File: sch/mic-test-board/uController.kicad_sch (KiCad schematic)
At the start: 43 parts, among them J1 CN11.male, J12 CN12.female, J5 CN12.male, J6 CN11.female, U34 SN74LVC126ARGYR, U5 NUCLEO144-H743ZI

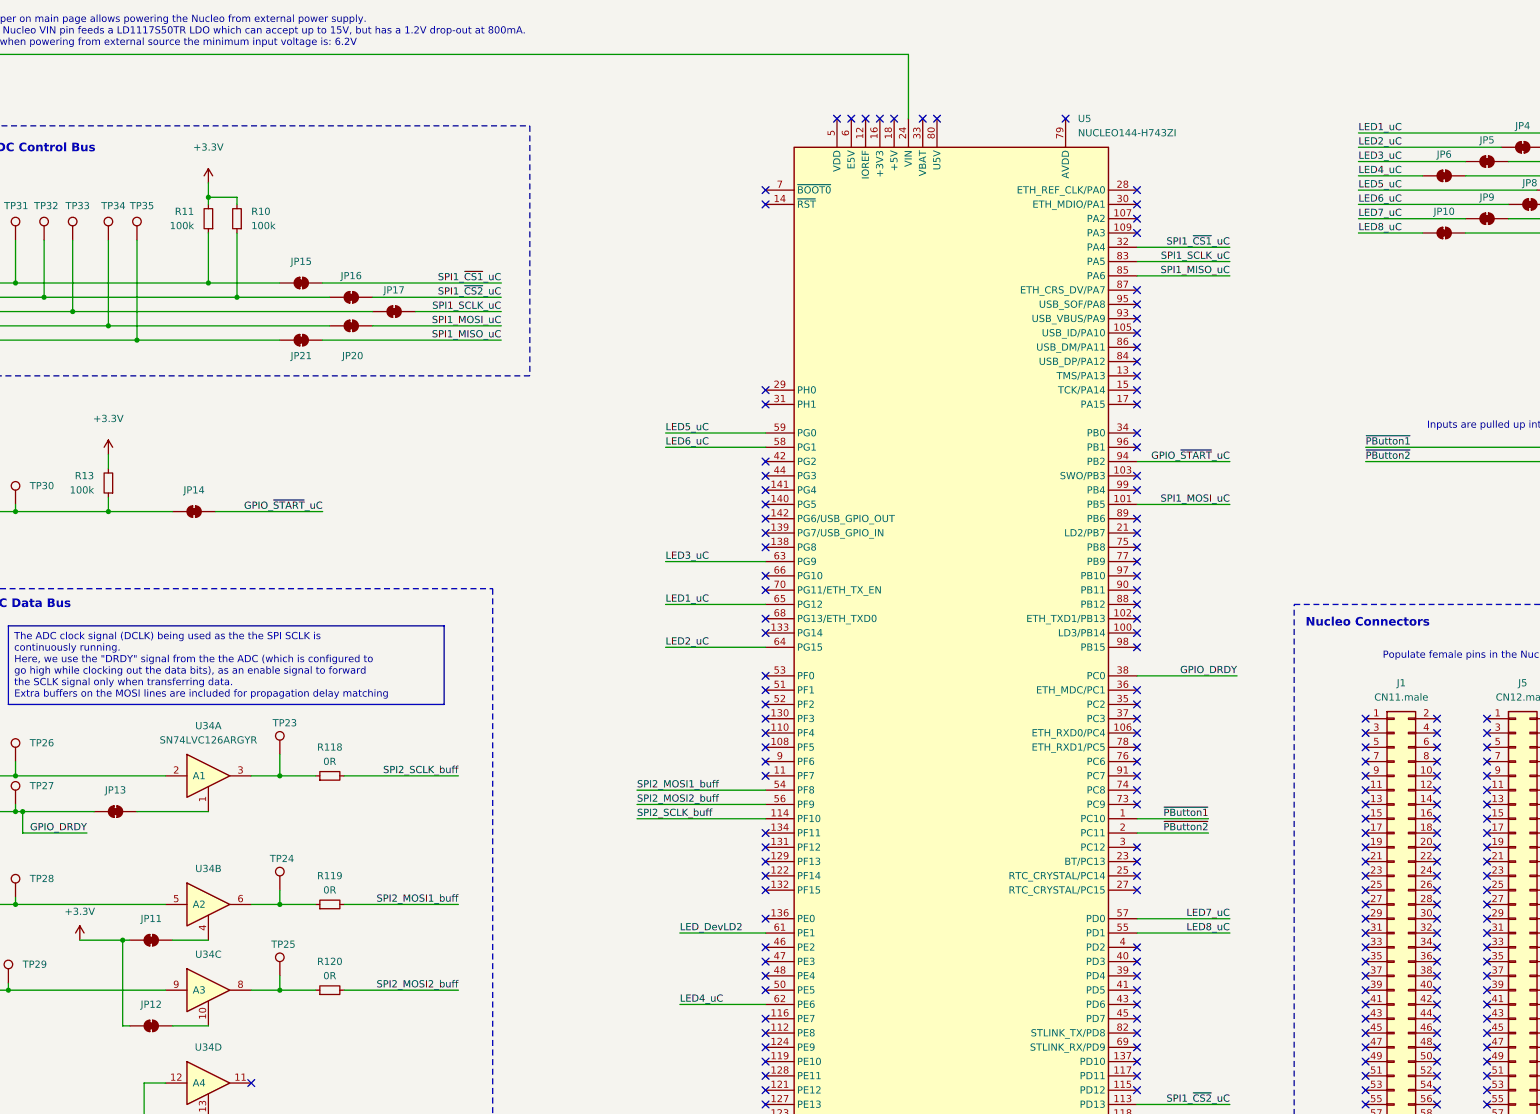
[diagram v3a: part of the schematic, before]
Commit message: sch: adding bringup notes
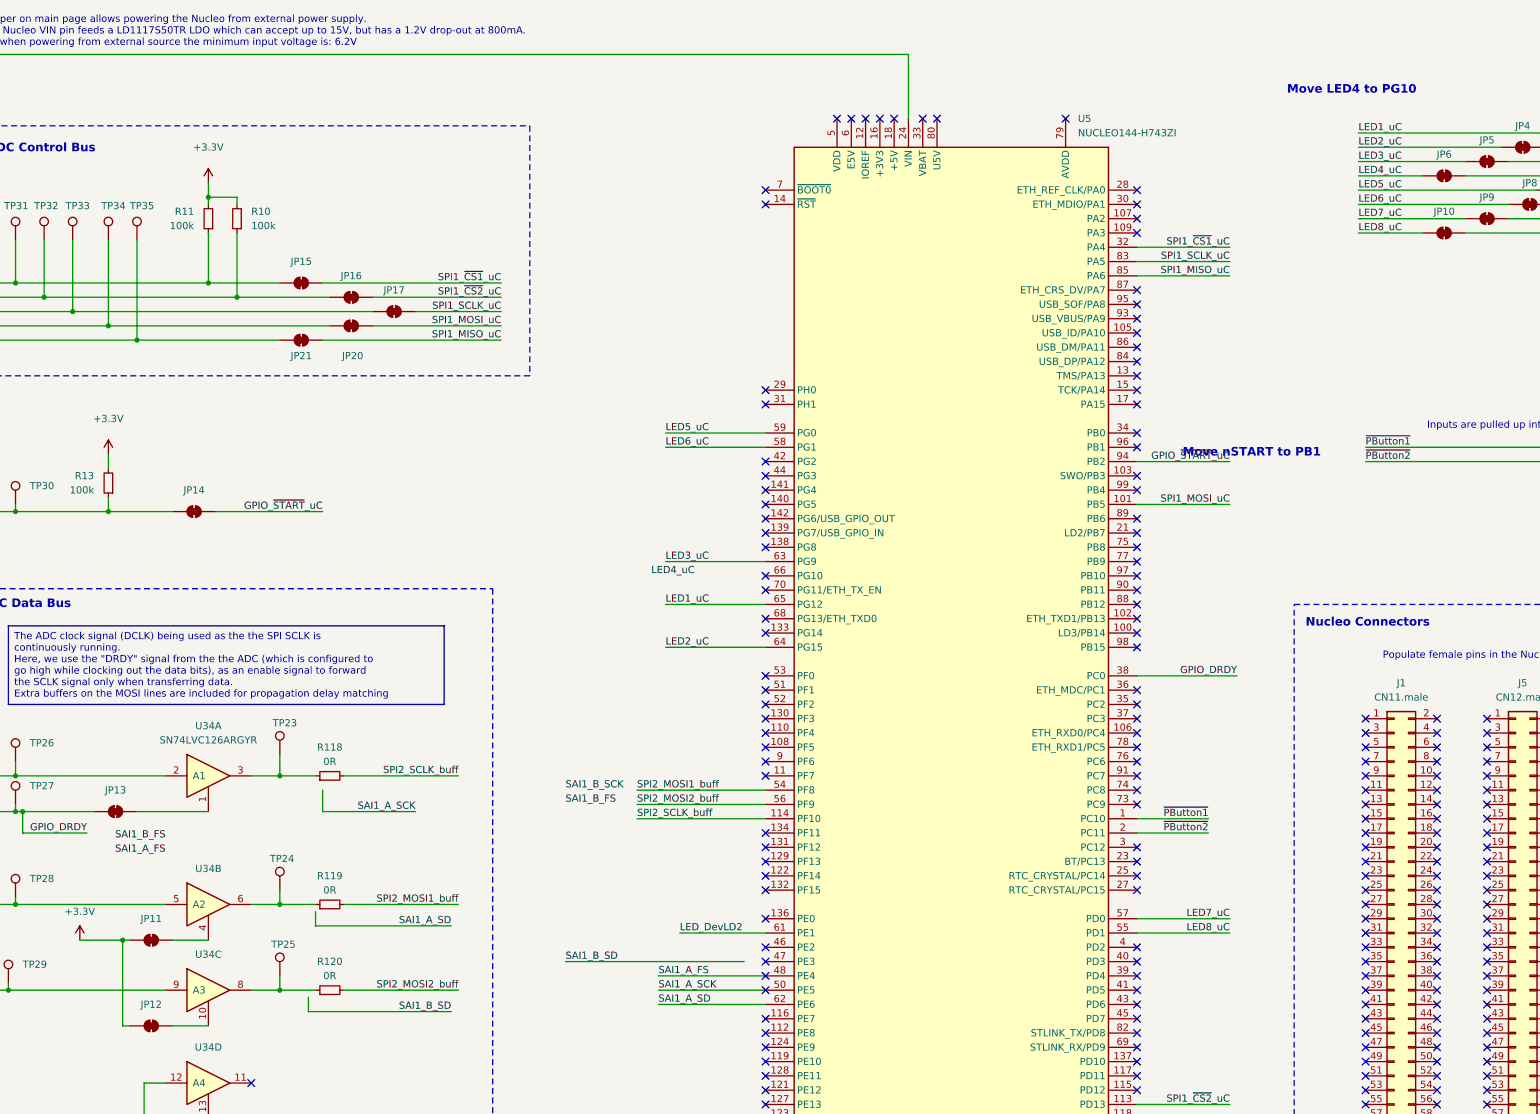
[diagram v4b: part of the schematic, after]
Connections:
- net LED4_uC: no longer U5.62 (PE6)
- net SAI1_A_FS: now reaches U5.48 (PE4)
- net SAI1_A_SCK: now reaches U5.50 (PE5)
- new net SAI1_A_SD: U5.62 (PE6)
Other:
- note added: "Move LED4 to PG10"
- note added: "Move nSTART to PB1"
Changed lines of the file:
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@@
+	(wire
+		(pts
+			(xy 170.18 190.5) (xy 201.93 190.5)
+		)
+		(stroke
+			(width 0)
+			(type default)
+		)
+	)
 	(wire
 		(pts
@@
 	(wire
 		(pts
+			(xy 127 160.02) (xy 127 163.83)
+		)
+		(stroke
+			(width 0)
+			(type default)
+		)
+	)
+	(wire
+		(pts
 			(xy 350.52 53.34) (xy 354.33 53.34)
 		)
@@
 	(wire
 		(pts
+			(xy 186.69 193.04) (xy 205.74 193.04)
+		)
+		(stroke
+			(width 0)
+			(type default)
+		)
+	)
+	(wire
+		(pts
 			(xy 182.88 162.56) (xy 205.74 162.56)
 		)
@@
 	(wire
 		(pts
+			(xy 186.69 195.58) (xy 205.74 195.58)
+		)
+		(stroke
+			(width 0)
+			(type default)
+		)
+	)
+	(wire
+		(pts
 			(xy 248.92 233.68) (xy 248.92 236.22)
 		)
@@
 	(wire
 		(pts
+			(xy 124.46 196.85) (xy 124.46 199.39)
+		)
+		(stroke
+			(width 0)
+			(type default)
+		)
+	)
+	(wire
+		(pts
 			(xy 72.39 162.56) (xy 72.39 163.83)
 		)
@@
 	(wire
 		(pts
+			(xy 149.86 184.15) (xy 125.73 184.15)
+		)
+		(stroke
+			(width 0)
+			(type default)
+		)
+	)
+	(wire
+		(pts
+			(xy 149.86 199.39) (xy 124.46 199.39)
+		)
+		(stroke
+			(width 0)
+			(type default)
+		)
+	)
+	(wire
+		(pts
 			(xy 95.25 212.09) (xy 95.25 218.44)
 		)
@@
 	(wire
 		(pts
-			(xy 190.5 198.12) (xy 205.74 198.12)
+			(xy 186.69 198.12) (xy 205.74 198.12)
 		)
 		(stroke
@@
 	(wire
 		(pts
+			(xy 125.73 181.61) (xy 125.73 184.15)
+		)
+		(stroke
+			(width 0)
+			(type default)
+		)
+	)
+	(wire
+		(pts
 			(xy 71.12 194.31) (xy 71.12 195.58)
 		)
@@
 		(pts
 			(xy 43.18 273.05) (xy 45.72 273.05)
+		)
+		(stroke
+			(width 0)
+			(type default)
+		)
+	)
+	(wire
+		(pts
+			(xy 143.51 163.83) (xy 127 163.83)
 		)
 		(stroke
@@
 		)
 	)
+	(text "Move LED4 to PG10"
+		(exclude_from_sim no)
+		(at 298.45 35.56 0)
+		(effects
+			(font
+				(size 1.524 1.524)
+				(thickness 0.3048)
+				(bold yes)
+			)
+			(justify left)
+		)
+	)
 	(text "Inputs are pulled up internally"
 		(exclude_from_sim no)
@@
 		)
 	)
+	(text "Move nSTART to PB1"
+		(exclude_from_sim no)
+		(at 279.908 100.076 0)
+		(effects
+			(font
+				(size 1.524 1.524)
+				(thickness 0.3048)
+				(bold yes)
+			)
+			(justify left)
+		)
+	)
 	(text "Nucleo Connectors"
 		(exclude_from_sim no)
@@
 		)
 	)
+	(label "SAI1_A_FS"
+		(at 99.06 171.45 180)
+		(fields_autoplaced yes)
+		(effects
+			(font
+				(size 1.27 1.27)
+			)
+			(justify right bottom)
+		)
+	)
 	(label "LED8_uC"
 		(at 311.15 60.96 0)
@@
 		)
 	)
-	(label "LED4_uC"
-		(at 190.5 198.12 0)
+	(label "SAI1_A_SD"
+		(at 186.69 198.12 0)
 		(fields_autoplaced yes)
 		(effects
@@
 		)
 	)
+	(label "SAI1_B_FS"
+		(at 170.18 162.56 0)
+		(fields_autoplaced yes)
+		(effects
+			(font
+				(size 1.27 1.27)
+			)
+			(justify left bottom)
+		)
+	)
 	(label "~{PButton1}"
 		(at 284.48 165.1 180)
@@
 		)
 	)
+	(label "LED4_uC"
+		(at 185.42 121.92 0)
+		(fields_autoplaced yes)
+		(effects
+			(font
+				(size 1.27 1.27)
+			)
+			(justify left bottom)
+		)
+	)
 	(label "SPI1_MISO_uC"
 		(at 288.29 68.58 180)
@@
 		)
 	)
+	(label "SAI1_A_SCK"
+		(at 143.51 163.83 180)
+		(fields_autoplaced yes)
+		(effects
+			(font
+				(size 1.27 1.27)
+			)
+			(justify right bottom)
+		)
+	)
+	(label "SAI1_A_FS"
+		(at 186.69 193.04 0)
+		(fields_autoplaced yes)
+		(effects
+			(font
+				(size 1.27 1.27)
+			)
+			(justify left bottom)
+		)
+	)
 	(label "LED6_uC"
 		(at 187.96 99.06 0)
@@
 		)
 	)
+	(label "SAI1_B_FS"
+		(at 99.06 168.91 180)
+		(fields_autoplaced yes)
+		(effects
+			(font
+				(size 1.27 1.27)
+			)
+			(justify right bottom)
+		)
+	)
+	(label "SAI1_B_SD"
+		(at 149.86 199.39 180)
+		(fields_autoplaced yes)
+		(effects
+			(font
+				(size 1.27 1.27)
+			)
+			(justify right bottom)
+		)
+	)
 	(label "SPI1_~{CS1}_uC"
 		(at 288.29 63.5 180)
@@
 		)
 	)
+	(label "SAI1_B_SCK"
+		(at 170.18 160.02 0)
+		(fields_autoplaced yes)
+		(effects
+			(font
+				(size 1.27 1.27)
+			)
+			(justify left bottom)
+		)
+	)
 	(label "SPI1_~{CS2}_uC"
 		(at 158.75 72.39 180)
@@
 		)
 	)
+	(label "SAI1_B_SD"
+		(at 170.18 190.5 0)
+		(fields_autoplaced yes)
+		(effects
+			(font
+				(size 1.27 1.27)
+			)
+			(justify left bottom)
+		)
+	)
 	(label "LED5_uC"
 		(at 311.15 53.34 0)
@@
 		)
 	)
+	(label "SAI1_A_SCK"
+		(at 186.69 195.58 0)
+		(fields_autoplaced yes)
+		(effects
+			(font
+				(size 1.27 1.27)
+			)
+			(justify left bottom)
+		)
+	)
+	(label "SAI1_A_SD"
+		(at 149.86 184.15 180)
+		(fields_autoplaced yes)
+		(effects
+			(font
+				(size 1.27 1.27)
+			)
+			(justify right bottom)
+		)
+	)
